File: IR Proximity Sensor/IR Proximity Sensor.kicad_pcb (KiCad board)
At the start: 2 copper layers, 39.4 x 22.4 mm, 9 parts, among them J1 Power & O/P Pins, U1 LM358

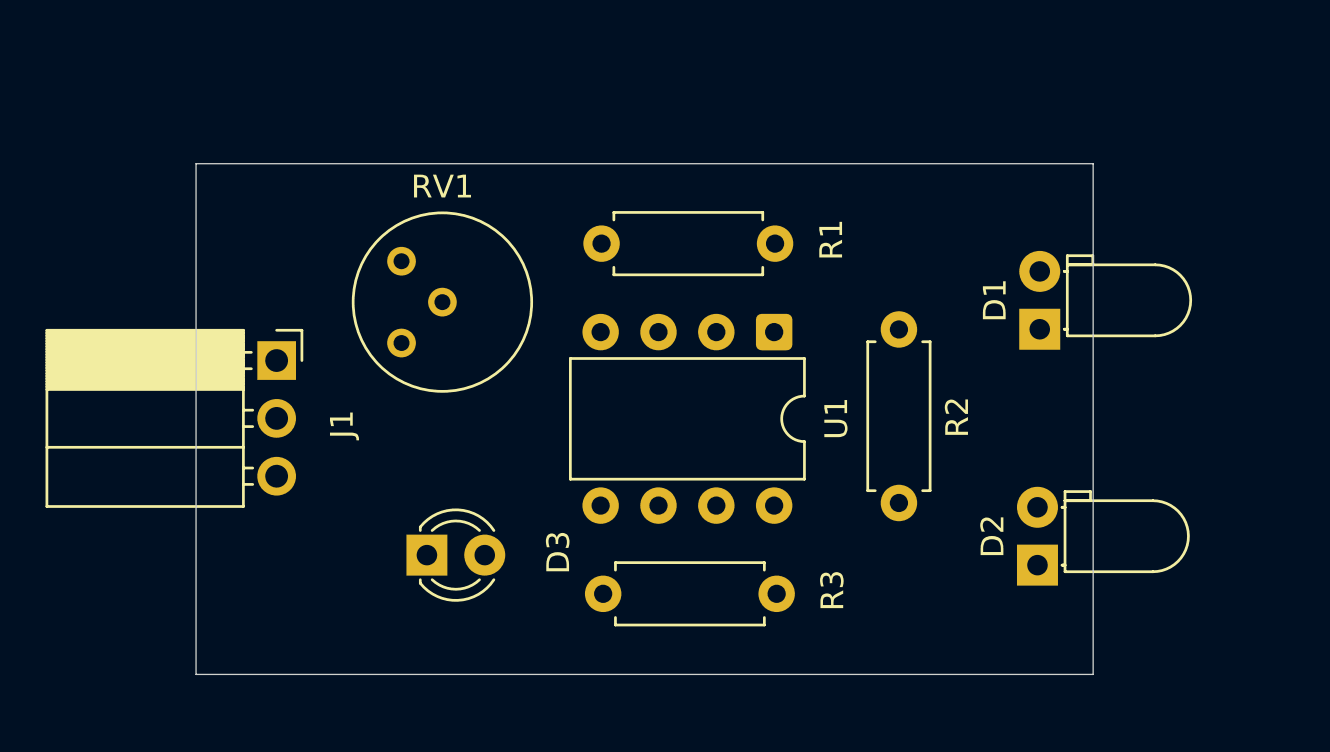
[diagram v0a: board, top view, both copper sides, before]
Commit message: Done with PCB routing and zone filling
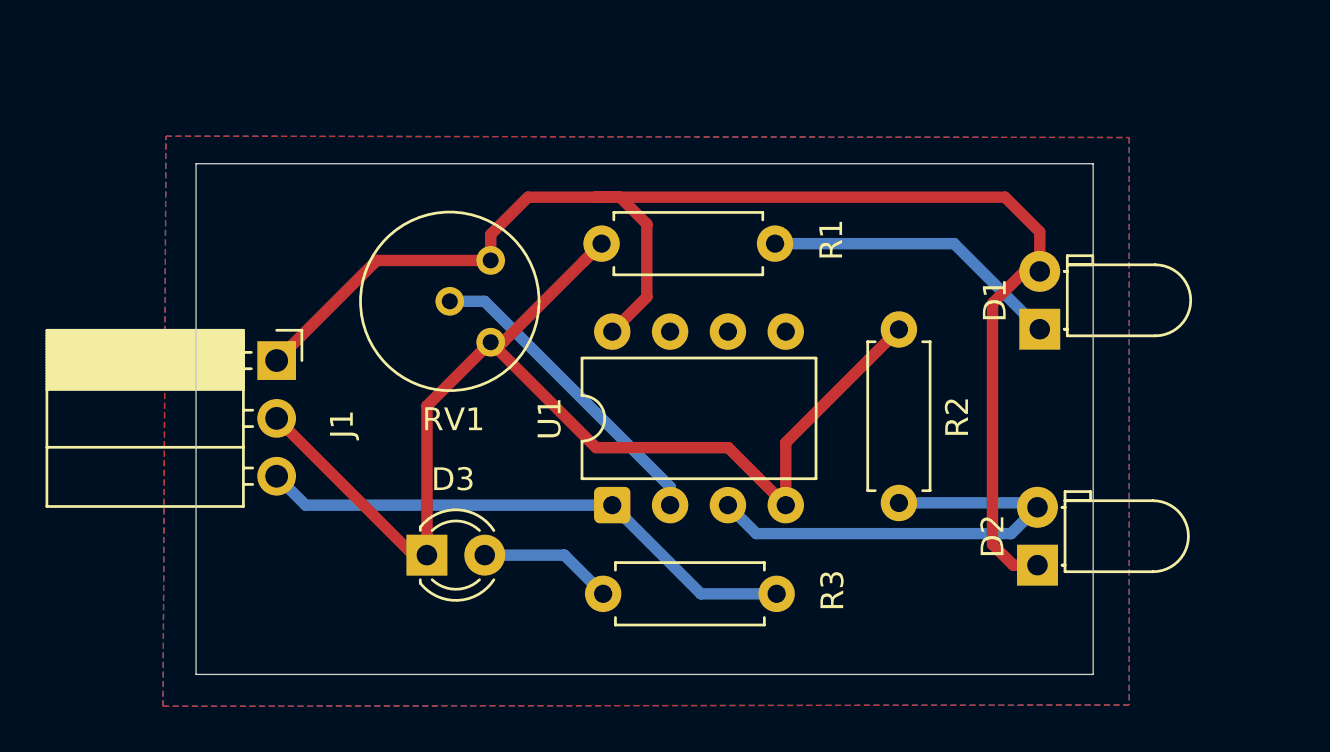
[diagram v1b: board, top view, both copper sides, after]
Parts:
- moved U1 10.4 mm to (136.4, 108.2), turned to 90 degrees
- moved RV1 5.34 mm to (131.1, 97.4), turned to 180 degrees
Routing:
- net +5V: track 0.00 -> 63.2 mm
- net GND: track 0.00 -> 53.1 mm
- net /OP: track 0.00 -> 24.1 mm
- net /NON_INV: track 0.00 -> 20.8 mm
- net /INV: track 0.00 -> 13.9 mm
- net Net-(D1-K): track 0.00 -> 13.2 mm
- net Net-(D3-A): track 0.00 -> 5.90 mm
- added copper zone on B.Cu, net GND
- added copper zone on F.Cu, net GND

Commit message: Updated footprints and PCB layout
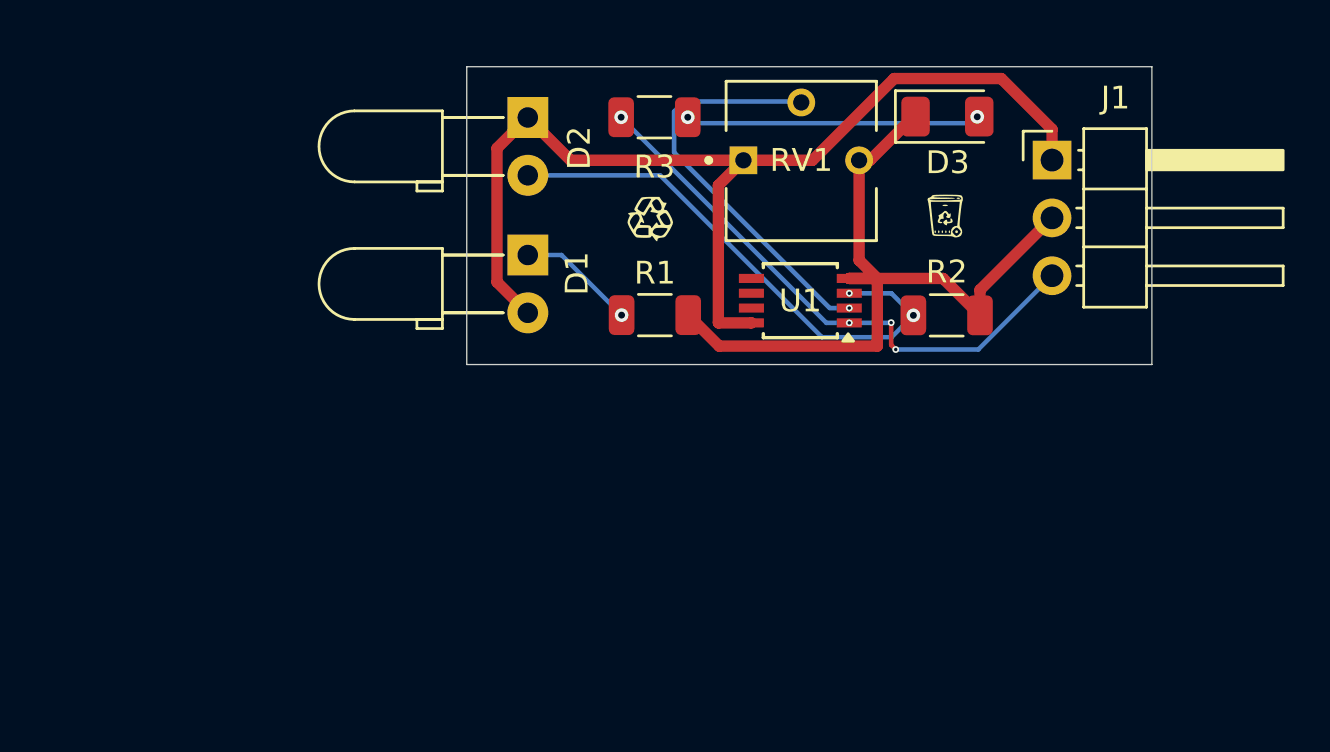
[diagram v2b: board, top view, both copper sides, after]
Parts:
- added G***: LOGO, LOGO, F.Cu at (151.1, 95.4)
- added G***: LOGO, LOGO, F.Cu at (138.1, 95.6)
- D1, D2: footprint LED_THT:LED_D3.0mm_Horizontal_O1.27mm_Z2.0mm_IRBlack -> LED_THT:LED_D3.0mm_Horizontal_O3.81mm_Z2.0mm
- D3: footprint LED_THT:LED_D3.0mm -> LED_SMD:LED_1206_3216Metric
- J1: value Power & O/P Pins -> Conn_01x03_Pin; footprint Connector_PinSocket_2.54mm:PinSocket_1x03_P2.54mm_Horizontal -> Connector_PinHeader_2.54mm:PinHeader_1x03_P2.54mm_Horizontal
- R1, R2, R3: footprint Resistor_THT:R_Axial_DIN0207_L6.3mm_D2.5mm_P7.62mm_Horizontal -> Resistor_SMD:R_1206_3216Metric
- RV1: footprint Potentiometer_THT:Potentiometer_Bourns_3339H_Vertical -> Potentiometer:TRIM_3362P-1-103
- U1: footprint Package_DIP:DIP-8_W7.62mm -> Package_SO:TSSOP-8_3x3mm_P0.65mm
- moved J1 35.2 mm to (155.7, 93.0)
- moved D3 29.9 mm to (151.2, 91.1)
- moved D2 29.8 mm to (132.7, 91.2), turned to -90 degrees
- moved D1 22.7 mm to (132.7, 97.2), turned to -90 degrees
- moved R3 21.6 mm to (138.3, 91.2), turned to 0 degrees
- moved RV1 14.3 mm to (144.7, 93.0), turned to 0 degrees
- moved U1 12.2 mm to (144.7, 99.2), turned to 180 degrees
- moved R2 8.50 mm to (151.1, 99.8), turned to 0 degrees
- moved R1 6.14 mm to (138.3, 99.8), turned to 0 degrees
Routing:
- net GND: track 53.1 -> 33.8 mm
- net +5V: track 63.2 -> 46.3 mm
- net Net-(D1-K): track 13.2 -> 5.21 mm, vias 0 -> 1
- net Net-(D3-A): track 5.90 -> 12.9 mm, vias 0 -> 2
- net /INV: track 13.9 -> 18.3 mm, vias 0 -> 1
- net /NON_INV: track 20.8 -> 23.5 mm, vias 0 -> 2
- net /OP: track 24.1 -> 25.1 mm, vias 0 -> 4
- removed copper zone on B.Cu, net GND
- removed copper zone on F.Cu, net GND
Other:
- board size 39.4 x 22.4 mm -> 30.1 x 13.1 mm

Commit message: All new changes commited
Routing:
- added copper zone on B.Cu, net GND
- added copper zone on F.Cu, net GND
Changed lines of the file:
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@@
 		(net 7)
+	)
+	(zone
+		(net 4)
+		(net_name "GND")
+		(layers "F.Cu" "B.Cu")
+		(hatch edge 0.5)
+		(connect_pads
+			(clearance 0.5)
+		)
+		(min_thickness 0.25)
+		(filled_areas_thickness no)
+		(fill yes
+			(thermal_gap 0.5)
+			(thermal_bridge_width 0.5)
+		)
+		(polygon
+			(pts
+				(xy 161 88) (xy 161 103) (xy 129 103) (xy 129 88)
+			)
+		)
 	)
 	(embedded_fonts no)
